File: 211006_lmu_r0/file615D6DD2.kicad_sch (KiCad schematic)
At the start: 31 parts, among them J11 Conn_ARM_JTAG_SWD_10, J12 Conn_01x03, J13 Conn_02x03_Odd_Even, SW1 SW_Push, U9 STM32F103C8Tx, Y1 Crystal_GND24

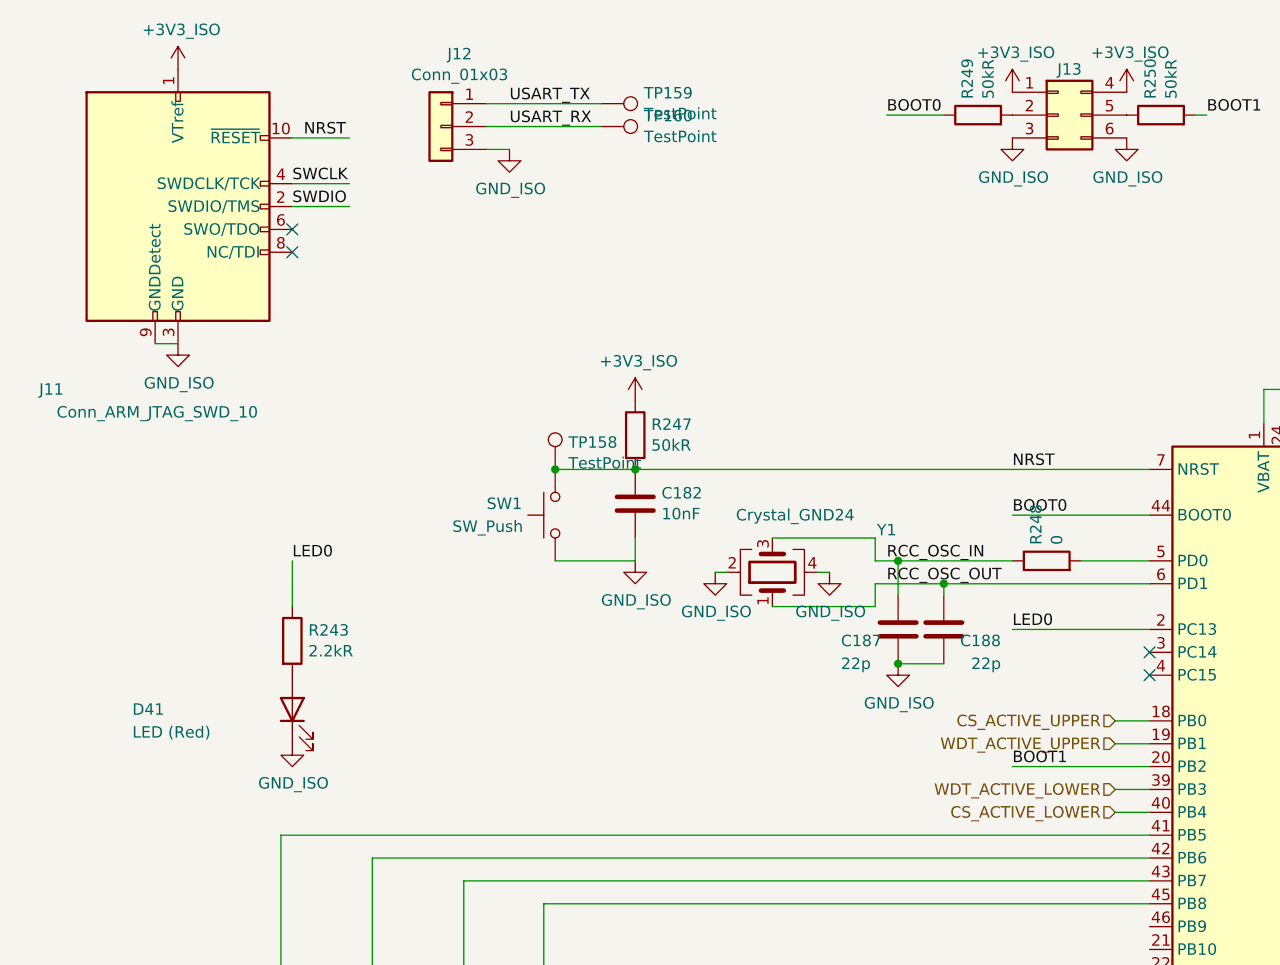
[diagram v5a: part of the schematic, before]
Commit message: routed ltc3811 accessories
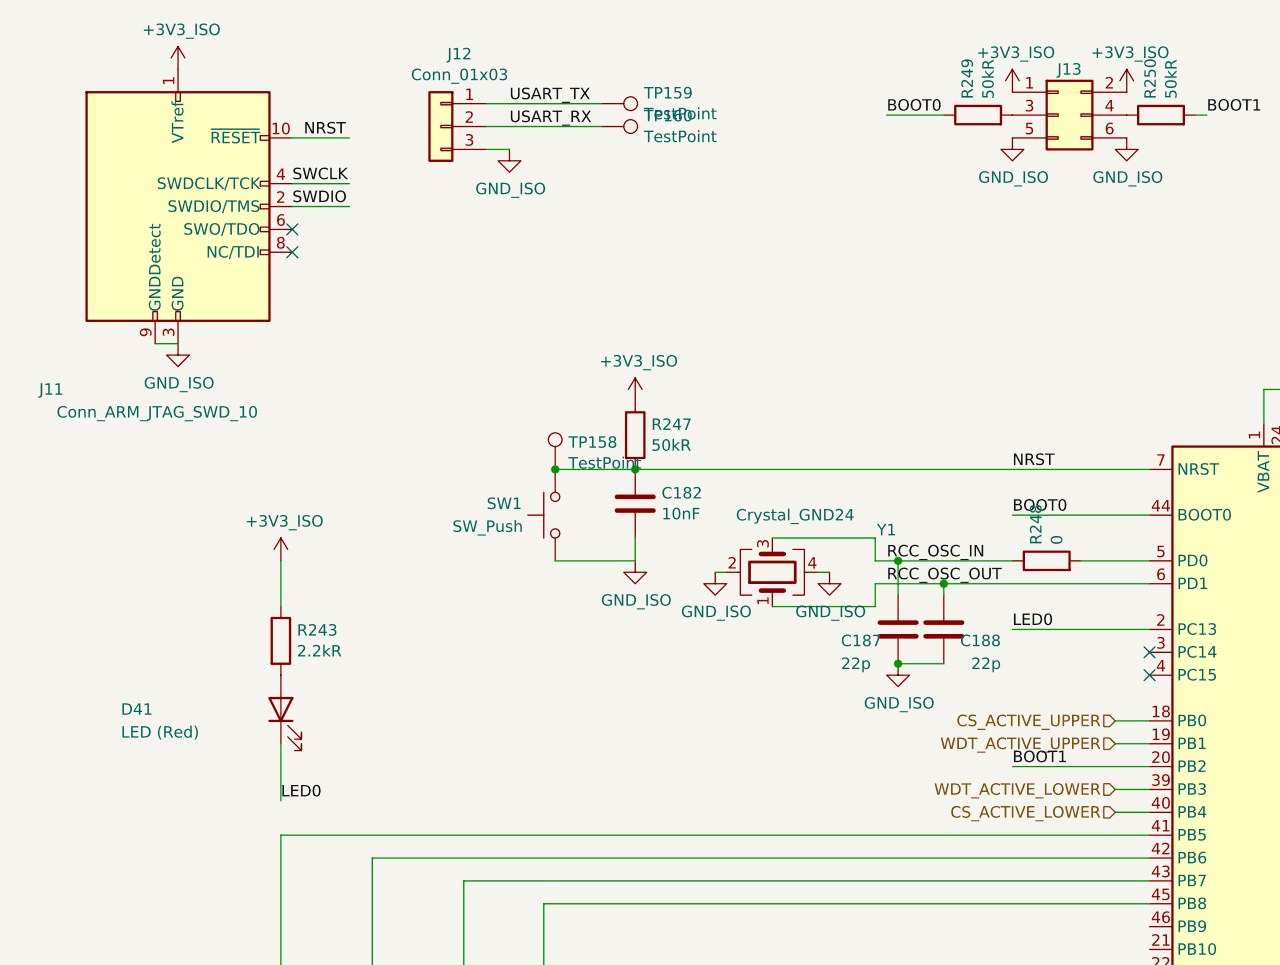
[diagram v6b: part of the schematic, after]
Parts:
- J13: symbol Connector_Generic:Conn_02x03_Top_Bottom -> Connector_Generic:Conn_02x03_Odd_Even
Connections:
- net +3V3_ISO: now also J13.2 (Pin_2), R243.1; no longer J13.4 (Pin_4)
- net GND_ISO: now also J13.5 (Pin_5); no longer D41.1 (K), J13.3 (Pin_3)
- net LED0: now also D41.1 (K); no longer R243.1
- net at R249.2: now also J13.3 (Pin_3); no longer J13.2 (Pin_2)
- net at R250.1: now also J13.4 (Pin_4); no longer J13.5 (Pin_5)
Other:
- moved on the sheet: D41, R243
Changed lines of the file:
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@@
     (stroke (width 0) (type default) (color 0 0 0 0))
   )
-  (wire (pts (xy 46.99 76.2) (xy 46.99 81.28))
+  (wire (pts (xy 45.72 76.2) (xy 45.72 81.28))
     (stroke (width 0) (type default) (color 0 0 0 0))
   )
@@
     (stroke (width 0) (type default) (color 0 0 0 0))
   )
+  (wire (pts (xy 45.72 96.52) (xy 45.72 102.87))
+    (stroke (width 0) (type default) (color 0 0 0 0))
+  )
   (wire (pts (xy 187.96 104.14) (xy 175.26 104.14))
     (stroke (width 0) (type default) (color 0 0 0 0))
@@
     (effects (font (size 1.27 1.27)) (justify left bottom))
   )
-  (label "LED0" (at 46.99 76.2 0)
+  (label "LED0" (at 45.72 102.87 0)
     (effects (font (size 1.27 1.27)) (justify left bottom))
   )
@@
     (pin "2")
   )
-  (symbol (lib_id "Device:R") (at 46.99 85.09 0) (unit 1)
-    (in_bom yes) (on_board yes)
-    (property "Reference" "R243" (id 0) (at 48.768 83.9216 0)
-      (effects (font (size 1.27 1.27)) (justify left))
-    )
-    (property "Value" "2.2kR" (id 1) (at 48.768 86.233 0)
-      (effects (font (size 1.27 1.27)) (justify left))
-    )
-    (property "Footprint" "Resistor_SMD:R_0603_1608Metric_Pad0.98x0.95mm_HandSolder" (id 2) (at 45.212 85.09 90)
-      (effects (font (size 1.27 1.27)) hide)
-    )
-    (property "Datasheet" "~" (id 3) (at 46.99 85.09 0)
-      (effects (font (size 1.27 1.27)) hide)
-    )
-    (property "Part Number" "-" (id 4) (at 46.99 85.09 0)
-      (effects (font (size 1.27 1.27)) hide)
-    )
-    (property "Manufacturer" "-" (id 5) (at 46.99 85.09 0)
-      (effects (font (size 1.27 1.27)) hide)
-    )
-    (pin "1")
-    (pin "2")
-  )
-  (symbol (lib_id "Device:LED") (at 46.99 92.71 90) (unit 1)
-    (in_bom yes) (on_board yes)
-    (property "Reference" "D41" (id 0) (at 29.21 92.71 90)
+  (symbol (lib_id "Device:R") (at 45.72 85.09 0) (unit 1)
+    (in_bom yes) (on_board yes)
+    (property "Reference" "R243" (id 0) (at 47.498 83.9216 0)
+      (effects (font (size 1.27 1.27)) (justify left))
+    )
+    (property "Value" "2.2kR" (id 1) (at 47.498 86.233 0)
+      (effects (font (size 1.27 1.27)) (justify left))
+    )
+    (property "Footprint" "Resistor_SMD:R_0603_1608Metric_Pad0.98x0.95mm_HandSolder" (id 2) (at 43.942 85.09 90)
+      (effects (font (size 1.27 1.27)) hide)
+    )
+    (property "Datasheet" "~" (id 3) (at 45.72 85.09 0)
+      (effects (font (size 1.27 1.27)) hide)
+    )
+    (property "Part Number" "-" (id 4) (at 45.72 85.09 0)
+      (effects (font (size 1.27 1.27)) hide)
+    )
+    (property "Manufacturer" "-" (id 5) (at 45.72 85.09 0)
+      (effects (font (size 1.27 1.27)) hide)
+    )
+    (pin "1")
+    (pin "2")
+  )
+  (symbol (lib_id "Device:LED") (at 45.72 92.71 90) (unit 1)
+    (in_bom yes) (on_board yes)
+    (property "Reference" "D41" (id 0) (at 27.94 92.71 90)
       (effects (font (size 1.27 1.27)) (justify right))
     )
-    (property "Value" "LED (Red)" (id 1) (at 29.21 95.25 90)
+    (property "Value" "LED (Red)" (id 1) (at 27.94 95.25 90)
       (effects (font (size 1.27 1.27)) (justify right))
     )
-    (property "Footprint" "LED_SMD:LED_0805_2012Metric_Pad1.15x1.40mm_HandSolder" (id 2) (at 46.99 92.71 0)
-      (effects (font (size 1.27 1.27)) hide)
-    )
-    (property "Datasheet" "~" (id 3) (at 46.99 92.71 0)
-      (effects (font (size 1.27 1.27)) hide)
-    )
-    (property "Manufacturer" "AMS OSRAM" (id 4) (at 46.99 92.71 0)
-      (effects (font (size 1.27 1.27)) hide)
-    )
-    (property "Mouser Part Number" "720-LSR976-NR-1" (id 5) (at 46.99 92.71 0)
-      (effects (font (size 1.27 1.27)) hide)
-    )
-    (property "Mouser URL" "https://au.mouser.com/ProductDetail/ams-OSRAM/LS-R976-NR-1-0-20-R18?qs=sGAEpiMZZMt82OzCyDsLFGbrp1fQkD8H8bij58Oys9s%3D" (id 6) (at 46.99 92.71 0)
-      (effects (font (size 1.27 1.27)) hide)
-    )
-    (property "Part Number" "LS R976-NR-1-0-20-R18" (id 7) (at 46.99 92.71 0)
-      (effects (font (size 1.27 1.27)) hide)
-    )
-    (pin "1")
-    (pin "2")
-  )
-  (symbol (lib_name "GND_ISO_15") (lib_id "gnd_iso:GND_ISO") (at 46.99 96.52 0) (unit 1)
-    (in_bom yes) (on_board yes)
-    (property "Reference" "#PWR080" (id 0) (at 46.99 102.87 0)
-      (effects (font (size 1.27 1.27)) hide)
-    )
-    (property "Value" "GND_ISO" (id 1) (at 47.117 100.9142 0))
-    (property "Footprint" "" (id 2) (at 46.99 96.52 0)
-      (effects (font (size 1.27 1.27)) hide)
-    )
-    (property "Datasheet" "" (id 3) (at 46.99 96.52 0)
-      (effects (font (size 1.27 1.27)) hide)
-    )
-    (pin "1")
+    (property "Footprint" "LED_SMD:LED_0805_2012Metric_Pad1.15x1.40mm_HandSolder" (id 2) (at 45.72 92.71 0)
+      (effects (font (size 1.27 1.27)) hide)
+    )
+    (property "Datasheet" "~" (id 3) (at 45.72 92.71 0)
+      (effects (font (size 1.27 1.27)) hide)
+    )
+    (property "Manufacturer" "AMS OSRAM" (id 4) (at 45.72 92.71 0)
+      (effects (font (size 1.27 1.27)) hide)
+    )
+    (property "Mouser Part Number" "720-LSR976-NR-1" (id 5) (at 45.72 92.71 0)
+      (effects (font (size 1.27 1.27)) hide)
+    )
+    (property "Mouser URL" "https://au.mouser.com/ProductDetail/ams-OSRAM/LS-R976-NR-1-0-20-R18?qs=sGAEpiMZZMt82OzCyDsLFGbrp1fQkD8H8bij58Oys9s%3D" (id 6) (at 45.72 92.71 0)
+      (effects (font (size 1.27 1.27)) hide)
+    )
+    (property "Part Number" "LS R976-NR-1-0-20-R18" (id 7) (at 45.72 92.71 0)
+      (effects (font (size 1.27 1.27)) hide)
+    )
+    (pin "1")
+    (pin "2")
   )
   (symbol (lib_name "+3V3_ISO_3") (lib_id "+3v3_iso:+3V3_ISO") (at 127 24.13 0) (unit 1)
@@
     (pin "1")
   )
-  (symbol (lib_id "Connector_Generic:Conn_02x03_Top_Bottom") (at 132.08 26.67 0) (unit 1)
+  (symbol (lib_name "+3V3_ISO_2") (lib_id "+3v3_iso:+3V3_ISO") (at 45.72 76.2 0) (unit 1)
+    (in_bom yes) (on_board yes)
+    (property "Reference" "#PWR0107" (id 0) (at 45.72 80.01 0)
+      (effects (font (size 1.27 1.27)) hide)
+    )
+    (property "Value" "+3V3_ISO" (id 1) (at 46.101 71.8058 0))
+    (property "Footprint" "" (id 2) (at 45.72 76.2 0)
+      (effects (font (size 1.27 1.27)) hide)
+    )
+    (property "Datasheet" "" (id 3) (at 45.72 76.2 0)
+      (effects (font (size 1.27 1.27)) hide)
+    )
+    (pin "1")
+  )
+  (symbol (lib_id "Connector_Generic:Conn_02x03_Odd_Even") (at 132.08 26.67 0) (unit 1)
     (in_bom yes) (on_board yes)
     (property "Reference" "J13" (id 0) (at 133.35 21.59 0))

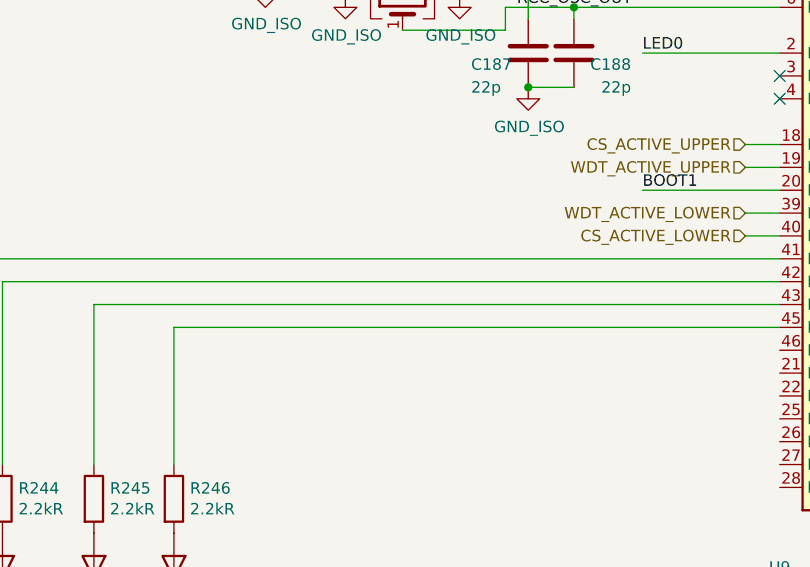
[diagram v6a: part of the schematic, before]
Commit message: silkscreen changes, shifting bun leds
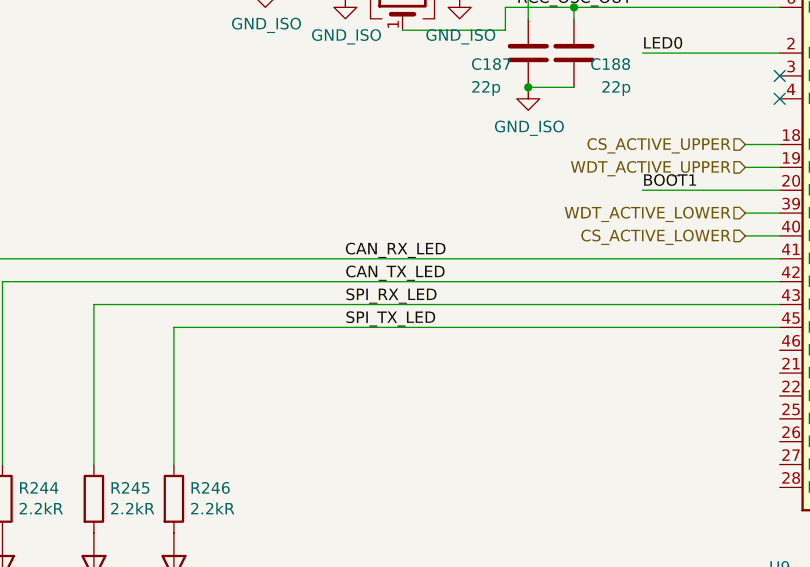
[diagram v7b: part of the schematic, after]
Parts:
- TP158, TP159, TP160: footprint TestPoint:TestPoint_Pad_D1.0mm -> custom:TestPoint_Pad_D1.0mm
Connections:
- net CAN_RX_LED: now reaches R242.1, U9.41 (PB5)
- net CAN_TX_LED: now reaches R244.1, U9.42 (PB6)
- net SPI_RX_LED: now reaches R245.1, U9.43 (PB7)
- net SPI_TX_LED: now reaches R246.1, U9.45 (PB8)
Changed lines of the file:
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@@
+    (effects (font (size 1.27 1.27)) (justify left bottom))
+  )
+  (label "CAN_TX_LED" (at 93.98 109.22 0)
     (effects (font (size 1.27 1.27)) (justify left bottom))
   )
@@
     (effects (font (size 1.27 1.27)) (justify left bottom))
   )
+  (label "SPI_RX_LED" (at 93.98 111.76 0)
+    (effects (font (size 1.27 1.27)) (justify left bottom))
+  )
+  (label "CAN_RX_LED" (at 93.937 106.68 0)
+    (effects (font (size 1.27 1.27)) (justify left bottom))
+  )
   (label "USART_TX" (at 177.8 99.06 0)
     (effects (font (size 1.27 1.27)) (justify left bottom))
@@
   )
   (label "BOOT0" (at 127 71.12 0)
+    (effects (font (size 1.27 1.27)) (justify left bottom))
+  )
+  (label "SPI_TX_LED" (at 93.98 114.3 0)
     (effects (font (size 1.27 1.27)) (justify left bottom))
   )
@@
       (effects (font (size 1.27 1.27)) (justify left))
     )
-    (property "Footprint" "TestPoint:TestPoint_Pad_D1.0mm" (id 2) (at 81.28 66.04 0)
+    (property "Footprint" "custom:TestPoint_Pad_D1.0mm" (id 2) (at 81.28 66.04 0)
       (effects (font (size 1.27 1.27)) hide)
     )
@@
       (effects (font (size 1.27 1.27)) (justify left))
     )
-    (property "Footprint" "TestPoint:TestPoint_Pad_D1.0mm" (id 2) (at 81.28 30.48 0)
+    (property "Footprint" "custom:TestPoint_Pad_D1.0mm" (id 2) (at 81.28 30.48 0)
       (effects (font (size 1.27 1.27)) hide)
     )
@@
       (effects (font (size 1.27 1.27)) (justify left))
     )
-    (property "Footprint" "TestPoint:TestPoint_Pad_D1.0mm" (id 2) (at 81.28 33.02 0)
-      (effects (font (size 1.27 1.27)) hide)
-    )
+    (property "Footprint" "custom:TestPoint_Pad_D1.0mm" (id 2) (at 81.28 33.02 0)
+      (effects (font (size 1.27 1.27)) hide)
+    )

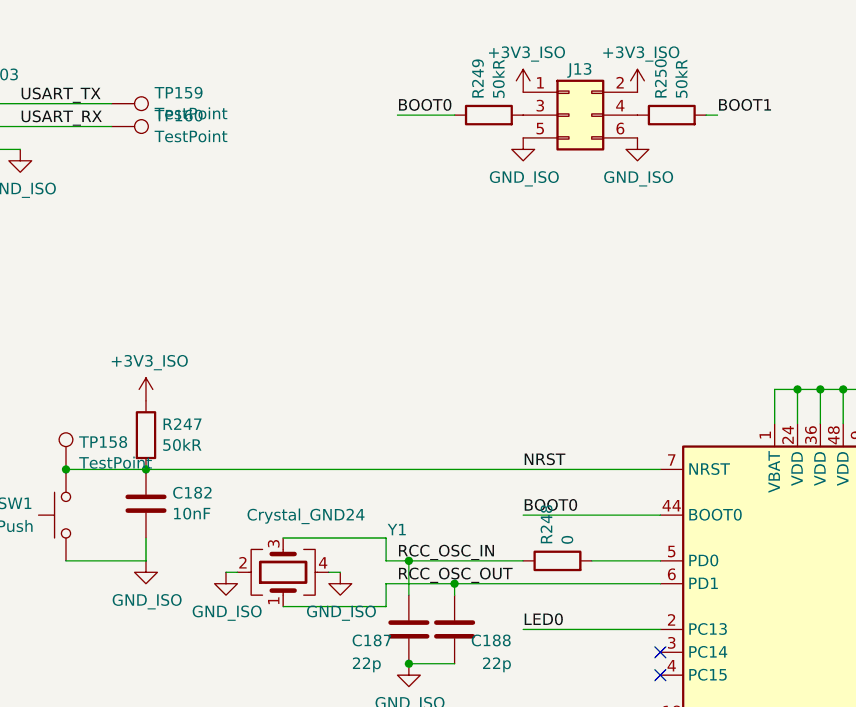
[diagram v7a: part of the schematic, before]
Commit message: going to bulk edit fields
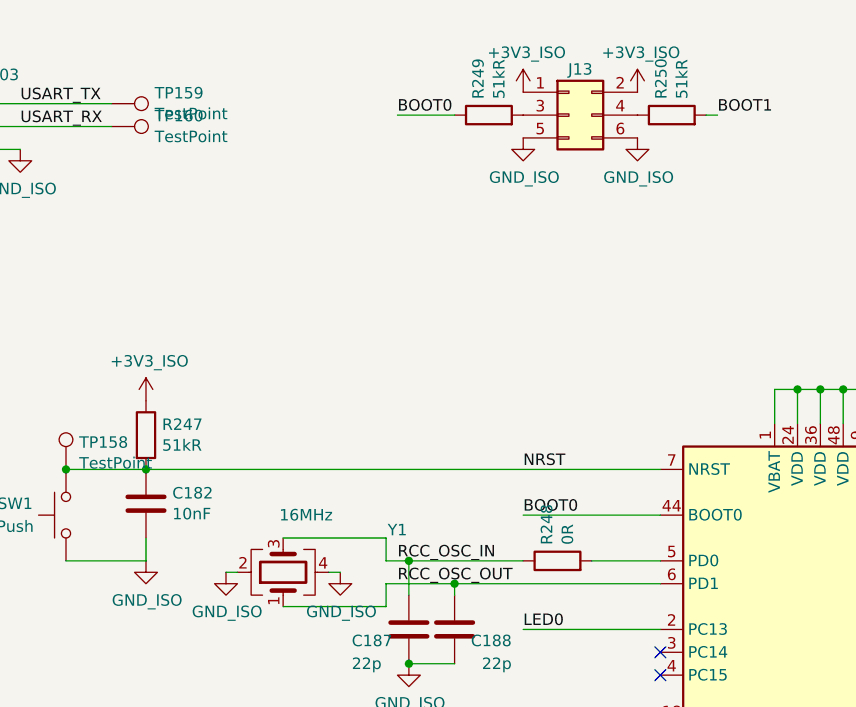
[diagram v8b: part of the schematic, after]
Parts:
- R247, R249, R250: value 50kR -> 51kR
- R248: value 0 -> 0R
- Y1: value Crystal_GND24 -> 16MHz
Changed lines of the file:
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@@
       (effects (font (size 1.27 1.27)) (justify left))
     )
-    (property "Value" "50kR" (id 1) (at 86.868 63.373 0)
+    (property "Value" "51kR" (id 1) (at 86.868 63.373 0)
       (effects (font (size 1.27 1.27)) (justify left))
     )
@@
       (effects (font (size 1.27 1.27)) (justify left))
     )
-    (property "Value" "50kR" (id 1) (at 124.333 24.892 0)
+    (property "Value" "51kR" (id 1) (at 124.333 24.892 0)
       (effects (font (size 1.27 1.27)) (justify left))
     )
@@
       (effects (font (size 1.27 1.27)) (justify left))
     )
-    (property "Value" "50kR" (id 1) (at 144.653 24.892 0)
+    (property "Value" "51kR" (id 1) (at 144.653 24.892 0)
       (effects (font (size 1.27 1.27)) (justify left))
     )
@@
     (in_bom yes) (on_board yes)
     (property "Reference" "Y1" (id 0) (at 113.03 72.771 90))
-    (property "Value" "Crystal_GND24" (id 1) (at 102.87 71.12 90))
+    (property "Value" "16MHz" (id 1) (at 102.87 71.12 90))
     (property "Footprint" "Crystal:Crystal_SMD_3225-4Pin_3.2x2.5mm_HandSoldering" (id 2) (at 100.33 77.47 0)
       (effects (font (size 1.27 1.27)) hide)
@@
       (effects (font (size 1.27 1.27)) (justify left))
     )
-    (property "Value" "0" (id 1) (at 131.953 74.422 0)
-      (effects (font (size 1.27 1.27)) (justify left))
-    )
+    (property "Value" "0R" (id 1) (at 131.953 74.422 0)
+      (effects (font (size 1.27 1.27)) (justify left))
+    )
